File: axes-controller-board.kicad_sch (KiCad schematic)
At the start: 79 parts, among them IC1 TPS5450QDDARQ1, J10 Conn_01x08, J11 Conn_01x04, J12 Conn_01x08, J13 Conn_01x04, J14 Conn_01x08, J15 Conn_01x08, J16 Conn_01x04, J17 Conn_01x08, J18 Conn_01x08, J19 Conn_01x04, J2 Conn_01x03, J20 Conn_01x08, J21 Conn_01x08, J22 Conn_01x04, J23 Conn_01x08, J24 Conn_01x08, J25 Conn_01x04, J26 Conn_01x08, J27 Raspberry_Pi_2_3, J28 DC1, J29 DC2, J3 Conn_01x03, J30 DC3, J31 Conn_01x08, J32 Conn_01x08, J33 DC1, J34 Conn_01x08, J35 Conn_01x08, J36 Conn_01x08, J37 ENDSTOP, J38 ENDSTOP, J39 ENDSTOP, J4 Conn_01x03, J40 Conn_01x03, J41 ENDSTOP, J42 ENDSTOP, J43 Conn_01x06, J9 Conn_01x08, U1 LM1117MP-3.3

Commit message: fix: prod notes
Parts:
- C1, C2, C3: LCSC C57112 -> C19702
- C12, C13, C15: value 0.01u -> 10n
- C41, C46: value 100nF -> 100n
- D1, D2: value LED -> LED_Small
- D3: JLCPCB Rotation Offset (none) -> 180
- IC1: JLCPCB Rotation Offset (none) -> 270
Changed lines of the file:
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@@
 			)
 		)
-		(property "Value" "0.01u"
+		(property "Value" "10n"
 			(at 227.33 46.9899 0)
 			(effects
@@
 			)
 		)
-		(property "Value" "0.01u"
+		(property "Value" "10n"
 			(at 283.21 35.5599 0)
 			(effects
@@
 			)
 		)
-		(property "Value" "100nF"
+		(property "Value" "100n"
 			(at 335.28 298.4499 0)
 			(effects
@@
 			)
 		)
-		(property "LCSC" "C57112"
+		(property "LCSC" "C19702"
 			(at 401.32 46.99 0)
 			(effects
@@
 			)
 		)
+		(property "JLCPCB Rotation Offset" "180"
+			(at 290.83 34.29 90)
+			(effects
+				(font
+					(size 1.27 1.27)
+				)
+				(hide yes)
+			)
+		)
 		(pin "1"
 		)
@@
 			)
 		)
-		(property "Value" "0.01u"
+		(property "Value" "10n"
 			(at 320.04 35.5599 0)
 			(effects
@@
 			)
 		)
-		(property "Value" "LED"
+		(property "Value" "LED_Small"
 			(at 426.72 52.3874 90)
 			(effects
@@
 			)
 		)
-		(property "Value" "100nF"
+		(property "Value" "100n"
 			(at 347.98 298.4499 0)
 			(effects
@@
 			)
 		)
+		(property "JLCPCB Rotation Offset" "270"
+			(at 236.22 39.37 0)
+			(effects
+				(font
+					(size 1.27 1.27)
+				)
+				(hide yes)
+			)
+		)
 		(pin "9"
 		)
@@
 			)
 		)
-		(property "Value" "LED"
+		(property "Value" "LED_Small"
 			(at 416.56 52.3874 90)
 			(effects
@@
 			)
 		)
-		(property "LCSC" "C57112"
+		(property "LCSC" "C19702"
 			(at 358.14 46.99 0)
 			(effects
@@
 			)
 		)
-		(property "LCSC" "C57112"
+		(property "LCSC" "C19702"
 			(at 392.43 46.99 0)
 			(effects

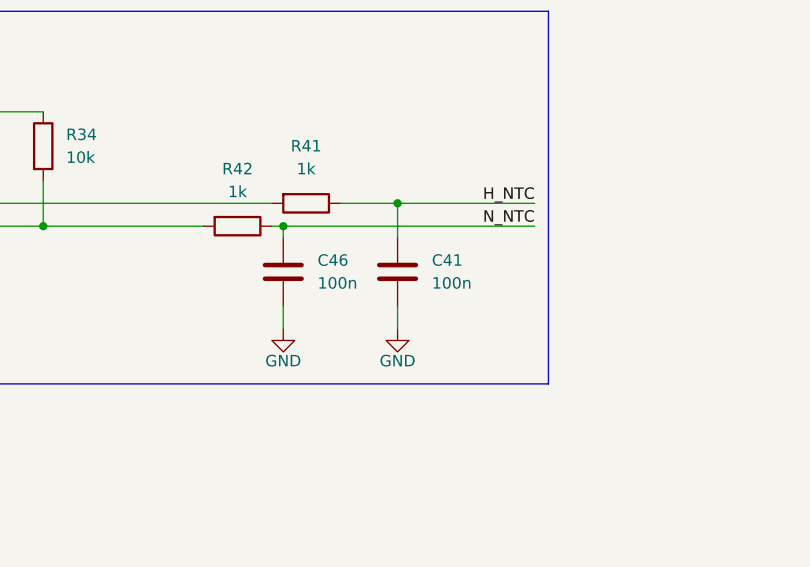
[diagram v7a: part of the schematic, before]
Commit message: fix: DNP for current sensors
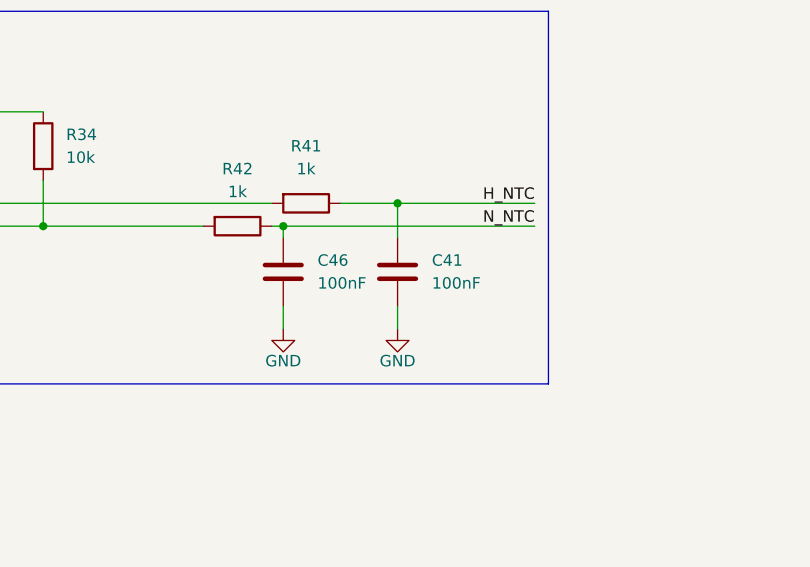
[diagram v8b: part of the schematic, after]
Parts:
- C41, C46: value 100n -> 100nF
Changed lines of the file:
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@@
 			)
 		)
-		(property "Value" "100n"
+		(property "Value" "100nF"
 			(at 335.28 298.4499 0)
 			(effects
@@
 			)
 		)
-		(property "Value" "100n"
+		(property "Value" "100nF"
 			(at 347.98 298.4499 0)
 			(effects
